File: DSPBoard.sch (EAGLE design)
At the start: 332 parts, among them IC1 AD1939WBSTZ, IC10 LM833D, IC11 LM833D, IC12 TL074D, IC2 25AA1024-I_SM, IC3 LM4040B10DBZ, IC4 LM833D, IC5 LM833D, IC6 LM833D, IC7 LM833D, IC8 LM833D, IC9 LM833D, U1 Value, U2 PEC11R-4315F-N0012, U3 PEC11R-4315F-N0012, X1 2510-, Y1 12.288MHz

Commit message: ready to do the board
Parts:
- added C132, C134: 100pF, rcl:C-EUC0805
- added C133, C135: 10nF, rcl:C-EUC0805
- added R154, R155, R156, R157, R158, R159, R160, R161, R162, R163, R164: 33R, rcl:R-EU_R0603
- C1, C18, C24, C5: value (none) -> 22uf; device rcl:C-EUC0603 -> rcl:CPOL-EU140CLH-0810
- C10, C13, C4, C7: value (none) -> 1uf
- C11, C14, C16, C19, C20, C21, C22, C23, C3, C30, C33, C34, C50, C51, C61, C62, C72, C73, C8: value (none) -> 100nf
- C12, C15, C17, C2, C25, C6, C9: value (none) -> 10nf
- C29: value (none) -> 47u
- C31: value (none) -> 22u
- C35, C52, C63, C74: value (none) -> 220uF; device rcl:C-EUC0805 -> rcl:CPOL-EU140CLH-1014
- C36, C53, C64, C75: value (none) -> 1nF
- C37, C54, C65, C76: value (none) -> 470p
- C38, C55, C66, C77: value (none) -> 1uF
- C39, C56, C67, C78: value (none) -> 100uF; device rcl:C-EUC0805 -> rcl:CPOL-EU140CLH-0810
- C46, C48, C57, C59, C68, C70: value (none) -> 100pF
- C47, C49, C58, C60, C69, C71: value (none) -> 10nF
- R1: value (none) -> 1k
- R11, R142, R18, R19, R20, R23, R24, R25, R26, R27, R29, R6, R7, R8: value (none) -> 33R
- R135: value (none) -> 562
- R31, R42, R55, R69: value (none) -> 15k
- R33, R43, R57, R70: value (none) -> 2.7k
- R35, R45, R62, R72: value (none) -> 2.2k
- R36, R46, R63, R73: value (none) -> 12.7k
- R37, R38, R39, R47, R48, R49, R5, R64, R65, R66, R74, R75, R76: value (none) -> 10k
- R4: value (none) -> 61.9k
- R40, R41, R50, R51, R67, R68, R77, R78: value (none) -> 22R
- U$11: value SDR1006-3R3ML -> SDR1006-3R3M-4.7uH
- U$12, U$8: value EEE-FK1C100R -> 1e5; device LM11173p3:EEE-FK1C100R -> rcl:CPOL-EU140CLH-0810
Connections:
- removed net N$34 (its old number): C53.2, IC5A.+IN, R43.2
- removed net N$36 (its old number): C52.2, IC5A.-IN, IC5A.OUT, R44.2, R51.2
- removed net N$50 (its old number): C63.2, IC6A.+IN, R57.2
- removed net N$51 (its old number): C62.2, IC6A.-IN, IC6A.OUT, R61.2, R68.2
- removed net N$61 (its old number): C73.2, IC7A.+IN, R70.2
- removed net N$62 (its old number): C72.2, IC7A.-IN, IC7A.OUT, R71.2, R78.2
- removed net VEE: C10.1, C11.1, C12.1, C13.1, C14.1, C15.1, C2.1, C3.1, C4.1, C5.1, C6.1, C7.1, C8.1, C9.1, U$1G$3.DVDD_20, U$1G$3.DVDD_35, U$1G$3.DVDD_53, U$1G$3.DVDD_71, U$2.COLLECTOR_2,4
- new net N$153: C10.1, C11.1, C12.1, C13.1, C14.1, C15.1, C2.1, C3.1, C4.1, C5.+, C6.1, C7.1, C8.1, C9.1, U$1G$3.DVDD_20, U$1G$3.DVDD_35, U$1G$3.DVDD_53, U$1G$3.DVDD_71, U$2.COLLECTOR_2,4
- new net N$154: R154.2, U$1G$4.BCLK_IN1_60
- new net N$155: R155.2, U$1G$4.LRCLK_IN1/MP11_61
- new net N$156: R156.1, U$1G$4.BCLK_IN2_65
- new net N$157: R157.1, U$1G$4.SDATA_IN2_67
- new net N$158: R158.1, U$1G$4.BCLK_IN3_68
- new net N$159: R159.1, U$1G$4.SDATA_IN3_70
- new net N$160: R160.1, U$1G$4.LRCLK_IN2/MP12_66
- new net N$161: R161.1, U$1G$4.LRCLK_IN3/MP13_69
- new net N$162: R162.1, U$1G$5.MP7_46
- new net N$163: R163.1, U$1G$5.BCLK_OUT3_51
- new net N$164: R164.2, U$1G$5.BCLK_OUT1_43
- new net N$38: C55.2, IC5B.+IN, R46.1
- new net N$42: C55.1, C56.+, R46.2, R47.2, R48.1, R49.1
- new net N$52: C66.2, IC6B.+IN, R63.1
- new net N$53: C66.1, C67.+, R63.2, R64.2, R65.1, R66.1
- new net N$63: C77.2, IC7B.+IN, R73.1
- new net N$64: C77.1, C78.+, R73.2, R74.2, R75.1, R76.1
- net +12V: now also C50.1, C61.1, C72.1; no longer C49.1, C59.1, C69.1
- net +3V3: now also C1.+, C18.+, C24.+; no longer C1.1, C18.1, C24.1
- net -12V: now also C51.2, C62.2, C73.2; no longer C50.2, C60.2, C70.2
- net AIN0+: now also C47.2; no longer C47.1
- net AIN0-: now also C47.1; no longer C47.2
- net AIN1+: now also C58.2, C59.1; no longer C57.1, C58.1
- net AIN1-: now also C58.1; no longer C56.2
- net AIN2+: now also C69.2, C70.1; no longer C67.1, C68.1
- net AIN2-: now also C68.2, C69.1; no longer C66.2, C67.2
- net AIN3+: now also C133.2, C134.1, R77.1; no longer C76.2, C77.2, R78.1
- net AIN3-: now also C132.2, C133.1, R78.1; no longer C77.1, C78.1, R77.1
- net ENCODER0_1: now also R162.2; no longer U$1G$5.MP7_46
- net ENCODER1_0: now also R160.2; no longer U$1G$4.LRCLK_IN2/MP12_66
- net ENCODER1_1: now also R161.2; no longer U$1G$4.LRCLK_IN3/MP13_69
- net GND: now also C1.-, C18.-, C24.-, C5.-, C50.2, C51.1, C54.1, C61.2, C62.1, C65.1, C72.2, C76.1, U$21.1, U$21.3, U$5.1, U$5.3, U$6.1, U$6.3, U$7.1, U$7.3; no longer C1.2, C18.2, C24.2, C49.2, C5.2, C50.1, C53.1, C59.2, C60.1, C63.1, C69.2, C70.1
- net N$10: now also C35.+, C49.1; no longer C35.2
- net N$18: now also C39.+; no longer C39.1
- net N$19: now also C39.-; no longer C39.2
- net N$21: now also R52.2
- net N$23: now also C53.1, R42.2, R43.1, R49.2; no longer C51.1, U$5.2
- net N$25: now also C54.2, IC5A.+IN, R43.2; no longer C51.2, R42.1
- net N$26: now also C53.2, IC5A.-IN, IC5A.OUT, R44.2, R51.2; no longer C52.1, R42.2, R43.1, R49.2
- net N$43: now also C56.-, R47.1; no longer C54.2, IC5B.+IN, R46.1
- net N$44: now also C57.1, C59.2; no longer C54.1, C55.1, R46.2, R47.2, R48.1, R49.1
- net N$45: now also C52.-, C60.2, U$5.2; no longer C55.2, R47.1
- net N$46: now also C52.+, C60.1, R42.1; no longer C56.1, C58.2
- net N$47: now also C64.1, R55.2, R57.1, R66.2; no longer C61.1, U$6.2
- net N$48: now also C65.2, IC6A.+IN, R57.2; no longer C61.2, R55.1
- net N$49: now also C64.2, IC6A.-IN, IC6A.OUT, R61.2, R68.2; no longer C62.1, R55.2, R57.1, R66.2
- net N$54: now also C67.-, R64.1; no longer C64.2, IC6B.+IN, R63.1
- net N$55: now also C68.1, C70.2; no longer C64.1, C65.1, R63.2, R64.2, R65.1, R66.1
- net N$56: now also C63.-, C71.2, U$6.2; no longer C65.2, R64.1
- net N$57: now also C63.+, C71.1, R55.1; no longer C66.1, C68.2
- net N$58: now also C75.1, R69.2, R70.1, R76.2; no longer C71.1, U$7.2
- net N$59: now also C76.2, IC7A.+IN, R70.2; no longer C71.2, R69.1
- net N$60: now also C75.2, IC7A.-IN, IC7A.OUT, R71.2, R78.2; no longer C72.1, R69.2, R70.1, R76.2
- net N$65: now also C78.-, R74.1; no longer C74.2, IC7B.+IN, R73.1
- net N$66: now also C132.1, C134.2; no longer C74.1, C75.1, R73.2, R74.2, R75.1, R76.1
- net N$67: now also C135.2, C74.-, U$7.2; no longer C75.2, R74.1
- net N$68: now also C135.1, C74.+, R69.1; no longer C76.1, C78.2
- net N$9: now also C35.-, C49.2; no longer C35.1
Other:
- moved on the sheet: C10, C11, C12, C13, C14, C15, C16, C17, C19, C2, C20, C21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

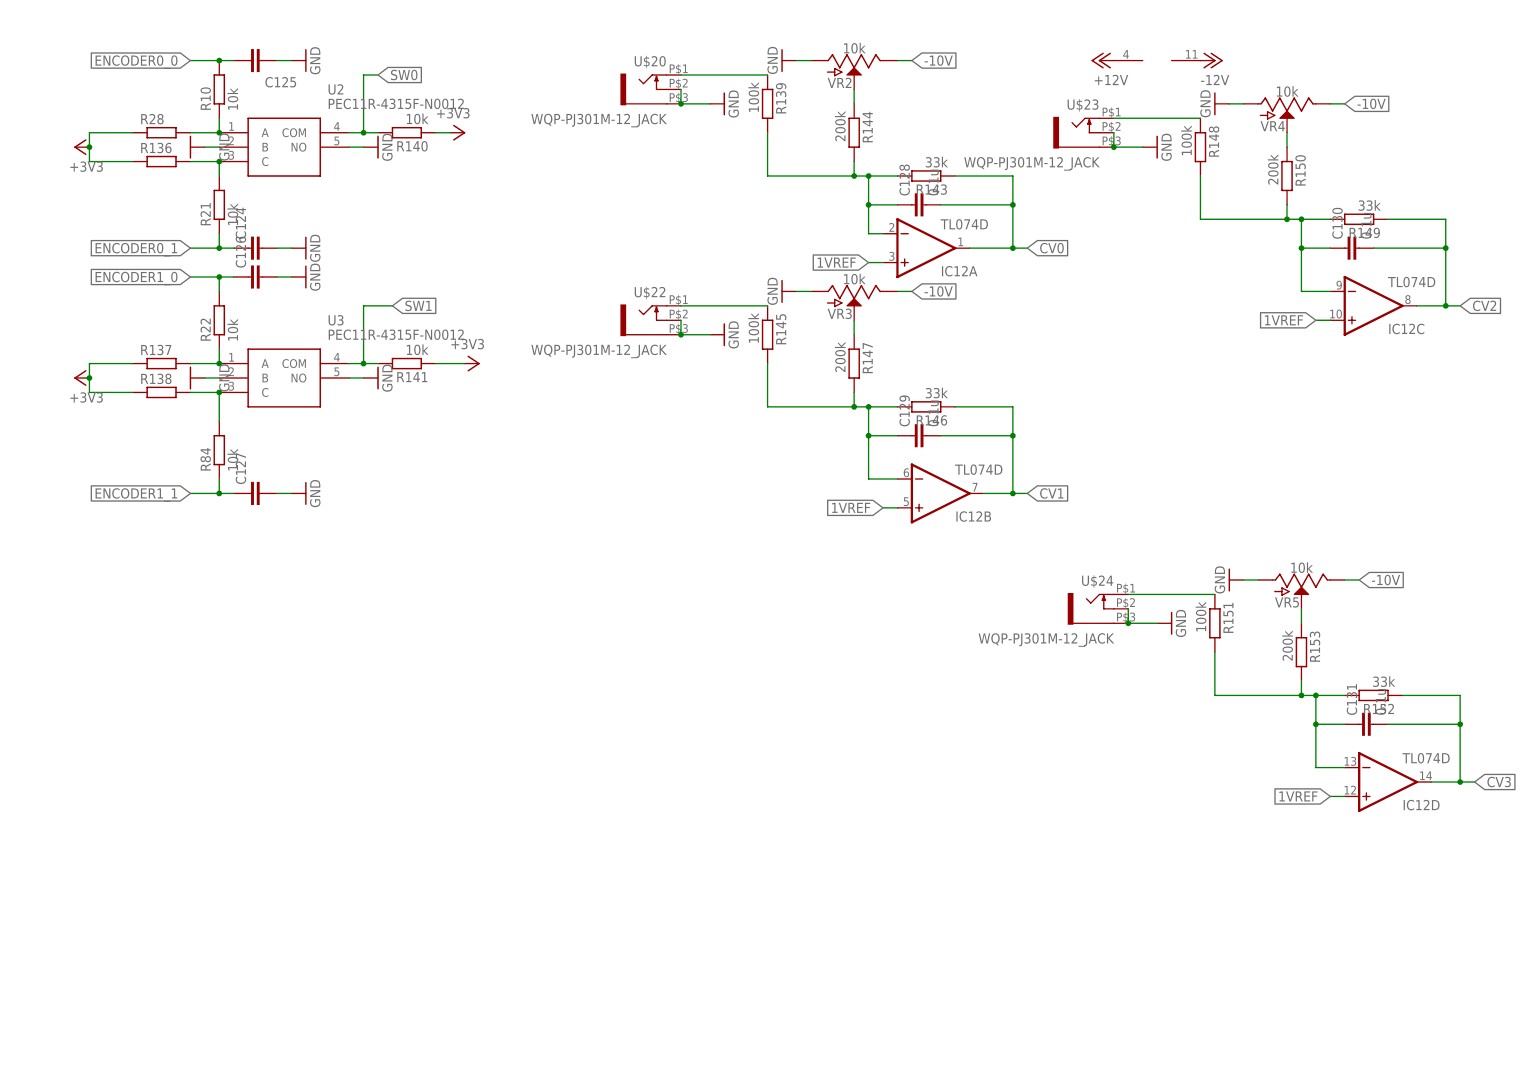
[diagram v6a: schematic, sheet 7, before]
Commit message: tidying up on daves recommendations
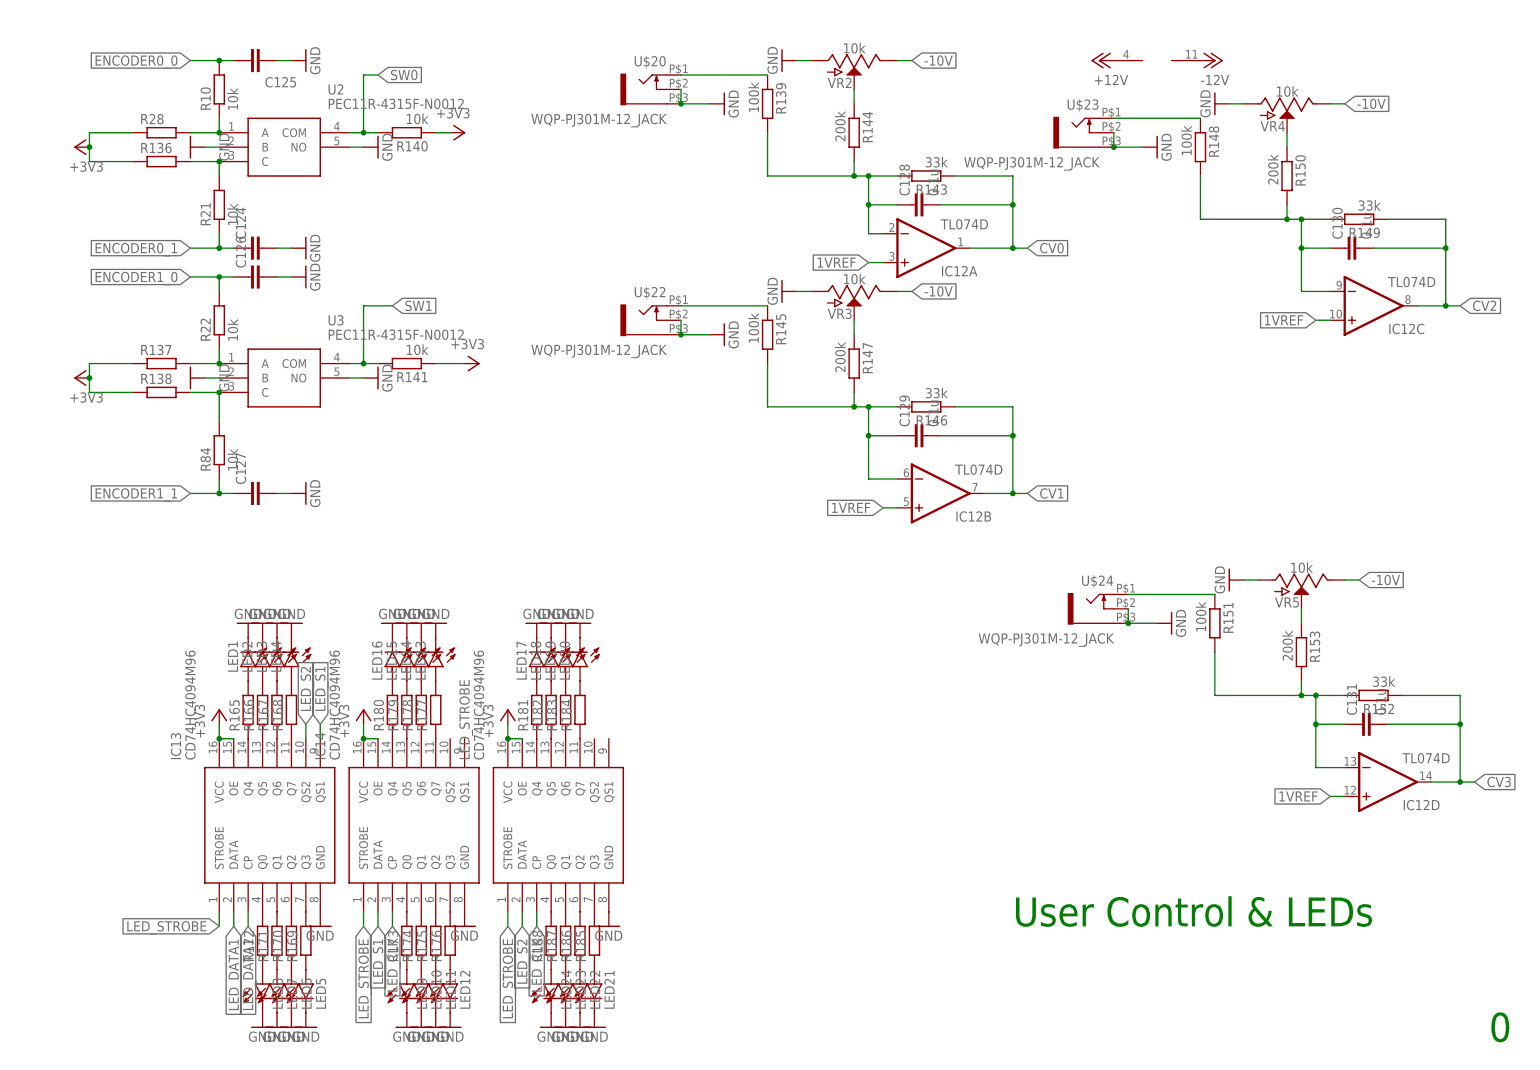
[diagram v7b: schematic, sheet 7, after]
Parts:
- removed C17, C25, C6: 10nf, rcl:C-EUC0603
- removed JP1: (no value), jumper:JP1Q
- removed R14: 10k, rcl:R-EU_R0603
- removed R15, R54: 33, rcl:R-EU_R0603
- removed R30: 480, rcl:R-EU_R0805
- removed R32: 10k, rcl:R-EU_R0805
- removed U$12, U$8: 1e5, rcl:CPOL-EU140CLH-0810
- removed VR1: (no value), v-reg:TL431CLP
- added C136: 100uF, rcl:CPOL-EU140CLH-0810
- added C137: 0.1uF, rcl:C-EUC0805
- added IC13, IC14, LED_STROBE: CD74HC4094M96, CD74HC4094M96:CD74HC4094M96
- added J1, J2, J3, J4: (no value), SparkFun-Connectors:CONN_01
- added LED1, LED10, LED11, LED12, LED13, LED14, LED15, LED16, LED17, LED18, LED19, LED2, LED20, LED21, LED22, LED23, LED24, LED3, LED4, LED5, LED6, LED7, LED8, LED9: (no value), led:LEDCHIPLED_0805
- added R165, R166, R167, R168, R169, R170, R171, R172, R173, R174, R175, R176, R177, R178, R179, R180, R181, R182, R183, R184, R185, R186, R187, R188: (no value), rcl:R-EU_R0805
- C1, C18, C24, C5: device rcl:CPOL-EU140CLH-0810 -> rcl:C-EUC0805
- C32: value 22u -> 0.1uF
- C45: value (none) -> 100n
- R12: value 100 -> 100R
- R13: value 33 -> 33R
- R16: value (none) -> 470
- U1: value Value -> LM11173.3NOPB
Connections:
- removed net ENCODER0_2: U$1G$1.AUXADC4_12
- removed net ENCODER1_2: U$1G$1.AUXADC5_13
- removed net N$153: C10.1, C11.1, C12.1, C13.1, C14.1, C15.1, C2.1, C3.1, C4.1, C5.+, C6.1, C7.1, C8.1, C9.1, U$1G$3.DVDD_20, U$1G$3.DVDD_35, U$1G$3.DVDD_53, U$1G$3.DVDD_71, U$2.COLLECTOR_2,4
- removed net N$31 (its old number): JP1.2, U$1G$2.SELFBOOT_34
- removed net N$32 (its old number): JP1.1, R14.1
- removed net N$33: R15.1, X1-1.KL
- removed net N$35: R54.1, X1-3.KL
- removed net SCL: R15.2
- removed net SDA: R54.2
- new net LED_CLK: IC14.CP, LED_STROBE.CP, R156.2
- new net LED_DATA1: IC13.CP, IC13.DATA, R157.2
- new net LED_DATA2: R159.2
- new net LED_S1: IC13.QS1, IC14.DATA
- new net LED_S2: IC13.QS2, LED_STROBE.DATA
- new net LED_STROBE: IC13.STROBE, IC14.STROBE, LED_STROBE.STROBE, R160.2
- new net N$152: IC13.Q4, R165.1
- new net N$165: IC13.Q5, R166.1
- new net N$166: IC13.Q6, R167.1
- new net N$167: IC13.Q7, R168.1
- new net N$168: IC13.Q3, R169.2
- new net N$169: IC13.Q2, R170.2
- new net N$170: IC13.Q1, R171.2
- new net N$171: IC13.Q0, R172.2
- new net N$172: IC14.Q0, R173.2
- new net N$173: IC14.Q1, R174.2
- new net N$174: IC14.Q2, R175.2
- new net N$175: IC14.Q3, R176.2
- new net N$176: IC14.Q7, R177.1
- new net N$177: IC14.Q6, R178.1
- new net N$178: IC14.Q5, R179.1
- new net N$179: IC14.Q4, R180.1
- new net N$180: LED_STROBE.Q4, R181.1
- new net N$181: LED_STROBE.Q5, R182.1
- new net N$182: LED_STROBE.Q6, R183.1
- new net N$183: LED_STROBE.Q7, R184.1
- new net N$184: LED_STROBE.Q3, R185.2
- new net N$185: LED_STROBE.Q2, R186.2
- new net N$186: LED_STROBE.Q1, R187.2
- new net N$187: LED_STROBE.Q0, R188.2
- new net N$188: LED1.A, R165.2
- new net N$189: LED2.A, R166.2
- new net N$190: LED3.A, R167.2
- new net N$191: LED4.A, R168.2
- new net N$192: LED5.A, R169.1
- new net N$193: LED6.A, R170.1
- new net N$194: LED7.A, R171.1
- new net N$195: LED8.A, R172.1
- new net N$196: LED9.A, R173.1
- new net N$197: LED10.A, R174.1
- new net N$198: LED11.A, R175.1
- new net N$199: LED12.A, R176.1
- new net N$200: LED13.A, R177.2
- new net N$201: LED14.A, R178.2
- new net N$202: LED15.A, R179.2
- new net N$203: LED16.A, R180.2
- new net N$204: LED17.A, R181.2
- new net N$205: LED18.A, R182.2
- new net N$206: LED19.A, R183.2
- new net N$207: LED20.A, R184.2
- new net N$208: LED21.A, R185.1
- new net N$209: LED22.A, R186.1
- new net N$210: LED23.A, R187.1
- new net N$211: LED24.A, R188.1
- new net N$212: C10.1, C11.1, C12.1, C13.1, C14.1, C15.1, C2.1, C3.1, C4.1, C5.1, C7.1, C8.1, C9.1, U$1G$3.DVDD_20, U$1G$3.DVDD_35, U$1G$3.DVDD_53, U$1G$3.DVDD_71, U$2.COLLECTOR_2,4
- net +12V: now also C136.+, C31.1; no longer C31.2
- net +3V3: now also C1.1, C18.1, C24.1, IC13.OE, IC13.VCC, IC14.OE, IC14.VCC, J4.1, LED_STROBE.OE, LED_STROBE.VCC, U$1G$2.SELFBOOT_34; no longer C1.+, C17.1, C18.+, C24.+, C25.1, R14.2
- net +5V: now also C32.1, J3.1; no longer R30.1, U$12.+
- net -10V: now also C45.2, J1.1; no longer C45.1
- net 1VREF: no longer C32.1, R30.2, R32.2, VR1.C, VR1.R
- net 3V3A: now also C137.1, J2.1; no longer U$8.+
- net ENCODER1_0: now also R155.1; no longer R160.2
- net GND: now also C1.2, C136.-, C137.2, C18.2, C24.2, C31.2, C45.1, C5.2, IC13.GND, IC14.GND, LED1.C, LED10.C, LED11.C, LED12.C, LED13.C, LED14.C, LED15.C, LED16.C, LED17.C, LED18.C, LED19.C, LED2.C, LED20.C, LED21.C, LED22.C, LED23.C, LED24.C, LED3.C, LED4.C, LED5.C, LED6.C, LED7.C, LED8.C, LED9.C, LED_STROBE.GND; no longer C1.-, C17.2, C18.-, C24.-, C25.2, C31.1, C45.2, C5.-, C6.2, R32.1, U$12.-, U$8.-, VR1.A
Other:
- note added: "0"
- note added: "Audio Input"
- note added: "Audio Output"
- note added: "DSP Power Supply Decoupling"
- note added: "Digital Connectivity & Codec"
- note added: "I2C, GPIO & Memory"
- note added: "User Control & LEDs"
- note removed: "1v2 supply"
- note removed: "3v3 Digital Supply"
- note removed: "5v5 Digital Supply"
- note removed: "TODO: Must remember to place the missing supply pins for the TL074 Must make 1v2 with voltage ref diode thing Must make 10v with voltage ref diode thing"
- moved on the sheet: C16, C2, C3, C31, C32, C4, C40, C41, C42, C43, C44, C45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

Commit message: more tidying
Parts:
- removed R154, R155, R156, R157, R158, R159, R160, R161, R163, R164: 33R, rcl:R-EU_R0603
- added C6: 1uF, rcl:C-EUC0805
- added R14: 100k, rcl:R-EU_R0805
- C119, C121: value 47u -> 22uF
- R11: value 33R -> 33r; device rcl:R-EU_R0603 -> rcl:R-EU_R0805
- R6, R7, R8: device rcl:R-EU_R0603 -> rcl:R-EU_R0805
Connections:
- removed net N$118: R7.2, U$1G$4.LRCLK_IN0/MP10_58
- removed net N$123: R11.2, U$1G$4.SDATA_IN1_62
- removed net N$142: R24.2
- removed net N$143: R25.2
- removed net N$144: R26.2
- removed net N$147: R29.2
- removed net N$154: R154.2, U$1G$4.BCLK_IN1_60
- removed net N$155: R155.2, U$1G$4.LRCLK_IN1/MP11_61
- removed net N$156: R156.1, U$1G$4.BCLK_IN2_65
- removed net N$157: R157.1, U$1G$4.SDATA_IN2_67
- removed net N$158: R158.1, U$1G$4.BCLK_IN3_68
- removed net N$159: R159.1, U$1G$4.SDATA_IN3_70
- removed net N$160: R160.1, U$1G$4.LRCLK_IN2/MP12_66
- removed net N$161: R161.1, U$1G$4.LRCLK_IN3/MP13_69
- removed net N$163: R163.1, U$1G$5.BCLK_OUT3_51
- removed net N$164: R164.2, U$1G$5.BCLK_OUT1_43
- new net N$33: R8.2, U$1G$4.LRCLK_IN0/MP10_58
- new net N$35: R6.2, U$1G$4.SDATA_IN1_62
- net +3V3: now also R14.2
- net ABCLK: now also R7.1; no longer R6.1
- net ALRCLK: now also R8.1; no longer R7.1
- net ASDATA1: now also R11.1; no longer R8.1
- net ASDATA2: now also R6.1; no longer R11.1
- net ENCODER1_0: now also U$1G$4.LRCLK_IN1/MP11_61; no longer R155.1
- net ENCODER1_1: now also U$1G$4.LRCLK_IN3/MP13_69; no longer R161.2
- net GND: now also C6.2
- net LED_CLK: now also R25.2; no longer R156.2
- net LED_DATA1: now also R26.2; no longer R157.2
- net LED_DATA2: now also R29.2; no longer R159.2
- net LED_STROBE: now also R24.2; no longer R160.2
- net N$120: now also R11.2; no longer R8.2
- net N$76: now also R7.2; no longer R6.2
- net RESET: now also C6.1, R14.1
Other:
- moved on the sheet: C111, C112, C114, C115, C116, C117, C118, C119, C122, R142, R162, R18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
